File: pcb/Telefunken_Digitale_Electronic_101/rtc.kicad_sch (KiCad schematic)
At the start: 5 parts, among them U3 DS3231

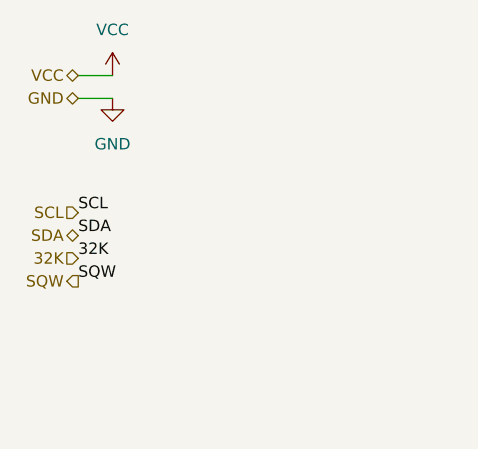
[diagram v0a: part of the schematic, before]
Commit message: SCH - rtc: adjusted footprints and direction of 32K label
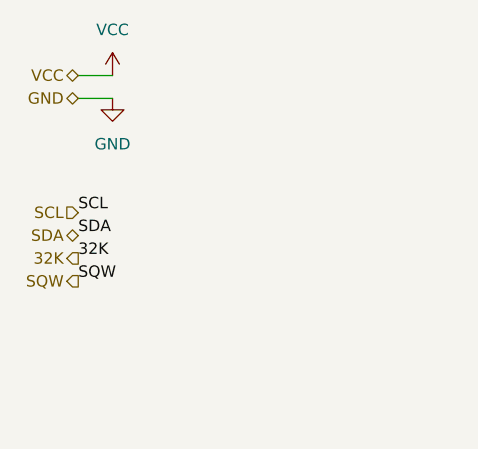
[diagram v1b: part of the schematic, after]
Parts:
- R10, R9: footprint Capacitor_SMD:C_0603_1608Metric_Pad1.08x0.95mm_HandSolder -> Resistor_SMD:R_0603_1608Metric_Pad0.98x0.95mm_HandSolder
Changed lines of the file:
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@@
 	)
 	(hierarchical_label "32K"
-		(shape input)
+		(shape output)
 		(at 38.1 77.47 180)
 		(effects
@@
 			)
 		)
-		(property "Footprint" "Capacitor_SMD:C_0603_1608Metric_Pad1.08x0.95mm_HandSolder"
+		(property "Footprint" "Resistor_SMD:R_0603_1608Metric_Pad0.98x0.95mm_HandSolder"
 			(at 136.652 78.74 90)
 			(hide yes)
@@
 			)
 		)
-		(property "Footprint" "Capacitor_SMD:C_0603_1608Metric_Pad1.08x0.95mm_HandSolder"
+		(property "Footprint" "Resistor_SMD:R_0603_1608Metric_Pad0.98x0.95mm_HandSolder"
 			(at 132.842 81.28 90)
 			(hide yes)

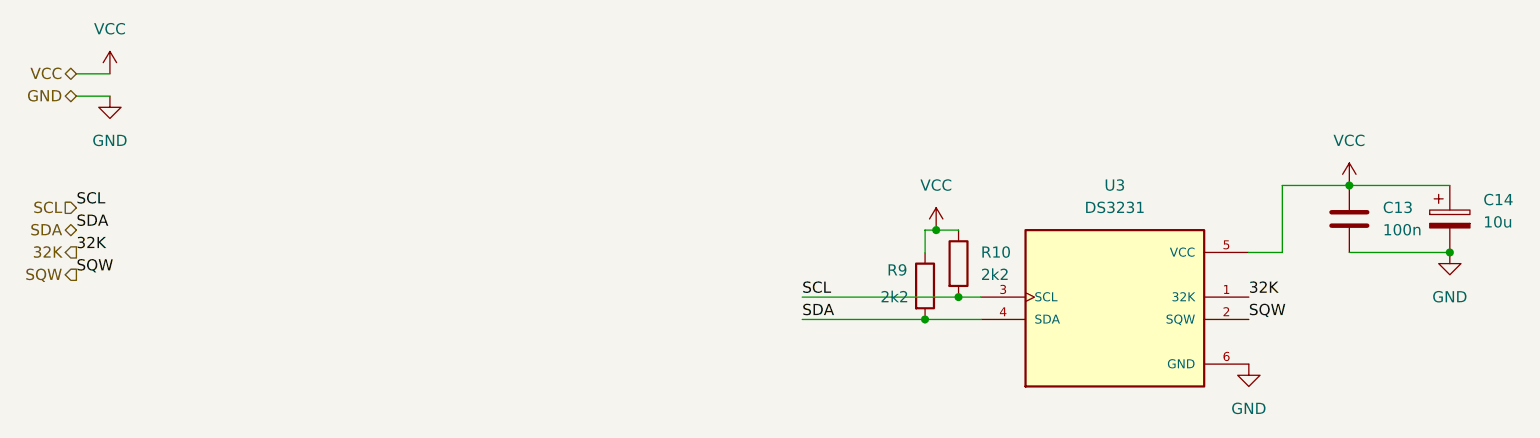
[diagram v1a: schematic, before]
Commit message: SCH and PCB: reannotated everything
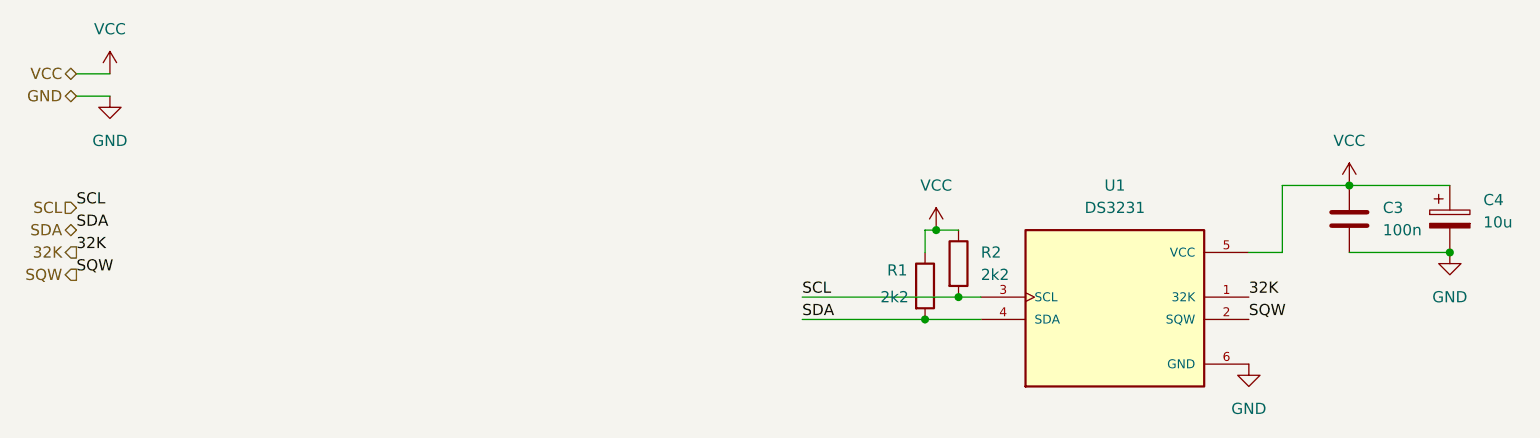
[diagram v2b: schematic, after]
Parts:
- renumbered C13 to C3, C14 to C4, R9 to R1, R10 to R2, U3 to U1
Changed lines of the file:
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@@
 		(dnp no)
 		(fields_autoplaced yes)
-		(property "Reference" "#PWR09"
+		(property "Reference" "#PWR013"
 			(at 194.31 83.82 0)
 			(hide yes)
@@
 			(project "Telefunken_Digitale_Electronic_101"
 				(path "/df1af5ff-c8b9-4769-9610-ead9e11e7e65/bbe7d115-46a0-489e-9136-389da3eb571d"
-					(reference "#PWR09")
+					(reference "#PWR013")
 					(unit 1)
 				)
@@
 		(dnp no)
 		(fields_autoplaced yes)
-		(property "Reference" "#PWR08"
+		(property "Reference" "#PWR012"
 			(at 182.88 73.66 0)
 			(hide yes)
@@
 			(project "Telefunken_Digitale_Electronic_101"
 				(path "/df1af5ff-c8b9-4769-9610-ead9e11e7e65/bbe7d115-46a0-489e-9136-389da3eb571d"
-					(reference "#PWR08")
+					(reference "#PWR012")
 					(unit 1)
 				)
@@
 		(dnp no)
 		(fields_autoplaced yes)
-		(property "Reference" "#PWR024"
+		(property "Reference" "#PWR09"
 			(at 41.91 66.04 0)
 			(hide yes)
@@
 			(project "Telefunken_Digitale_Electronic_101"
 				(path "/df1af5ff-c8b9-4769-9610-ead9e11e7e65/bbe7d115-46a0-489e-9136-389da3eb571d"
-					(reference "#PWR024")
+					(reference "#PWR09")
 					(unit 1)
 				)
@@
 		(dnp no)
 		(fields_autoplaced yes)
-		(property "Reference" "C13"
+		(property "Reference" "C3"
 			(at 186.69 72.3899 0)
 			(show_name no)
@@
 			(project "Telefunken_Digitale_Electronic_101"
 				(path "/df1af5ff-c8b9-4769-9610-ead9e11e7e65/bbe7d115-46a0-489e-9136-389da3eb571d"
-					(reference "C13")
+					(reference "C3")
 					(unit 1)
 				)
@@
 		(dnp no)
 		(fields_autoplaced yes)
-		(property "Reference" "#PWR019"
+		(property "Reference" "#PWR010"
 			(at 135.89 78.74 0)
 			(hide yes)
@@
 			(project "Telefunken_Digitale_Electronic_101"
 				(path "/df1af5ff-c8b9-4769-9610-ead9e11e7e65/bbe7d115-46a0-489e-9136-389da3eb571d"
-					(reference "#PWR019")
+					(reference "#PWR010")
 					(unit 1)
 				)
@@
 		(dnp no)
 		(fields_autoplaced yes)
-		(property "Reference" "R10"
+		(property "Reference" "R2"
 			(at 140.97 77.4699 0)
 			(show_name no)
@@
 			(project "Telefunken_Digitale_Electronic_101"
 				(path "/df1af5ff-c8b9-4769-9610-ead9e11e7e65/bbe7d115-46a0-489e-9136-389da3eb571d"
-					(reference "R10")
+					(reference "R2")
 					(unit 1)
 				)
@@
 		(dnp no)
 		(fields_autoplaced yes)
-		(property "Reference" "C14"
+		(property "Reference" "C4"
 			(at 198.12 71.5009 0)
 			(show_name no)
@@
 			(project "Telefunken_Digitale_Electronic_101"
 				(path "/df1af5ff-c8b9-4769-9610-ead9e11e7e65/bbe7d115-46a0-489e-9136-389da3eb571d"
-					(reference "C14")
+					(reference "C4")
 					(unit 1)
 				)
@@
 		(dnp no)
 		(fields_autoplaced yes)
-		(property "Reference" "U3"
+		(property "Reference" "U1"
 			(at 156.21 69.85 0)
 			(show_name no)
@@
 			(project "Telefunken_Digitale_Electronic_101"
 				(path "/df1af5ff-c8b9-4769-9610-ead9e11e7e65/bbe7d115-46a0-489e-9136-389da3eb571d"
-					(reference "U3")
+					(reference "U1")
 					(unit 1)
 				)
@@
 		(dnp no)
 		(fields_autoplaced yes)
-		(property "Reference" "#PWR010"
+		(property "Reference" "#PWR011"
 			(at 171.45 96.52 0)
 			(hide yes)
@@
 			(project "Telefunken_Digitale_Electronic_101"
 				(path "/df1af5ff-c8b9-4769-9610-ead9e11e7e65/bbe7d115-46a0-489e-9136-389da3eb571d"
-					(reference "#PWR010")
+					(reference "#PWR011")
 					(unit 1)
 				)
@@
 		(dnp no)
 		(fields_autoplaced yes)
-		(property "Reference" "#PWR023"
+		(property "Reference" "#PWR08"
 			(at 41.91 60.96 0)
 			(hide yes)
@@
 			(project "Telefunken_Digitale_Electronic_101"
 				(path "/df1af5ff-c8b9-4769-9610-ead9e11e7e65/bbe7d115-46a0-489e-9136-389da3eb571d"
-					(reference "#PWR023")
+					(reference "#PWR08")
 					(unit 1)
 				)
@@
 		(in_pos_files yes)
 		(dnp no)
-		(property "Reference" "R9"
+		(property "Reference" "R1"
 			(at 130.302 79.502 0)
 			(show_name no)
@@
 			(project "Telefunken_Digitale_Electronic_101"
 				(path "/df1af5ff-c8b9-4769-9610-ead9e11e7e65/bbe7d115-46a0-489e-9136-389da3eb571d"
-					(reference "R9")
-					(unit 1)
-				)
+					(reference "R1")
+					(unit 1)
+				)

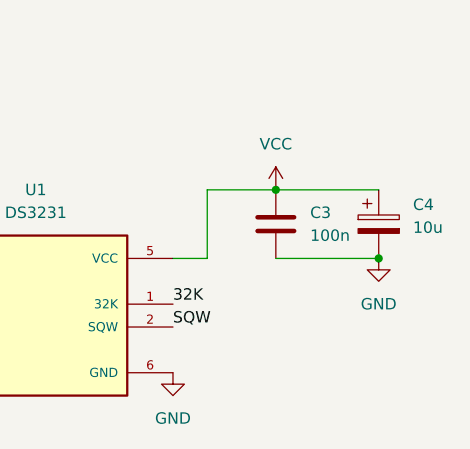
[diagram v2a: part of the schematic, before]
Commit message: adjusted connectors footprints, added footprint to input polarized capacitor, rtc and display polarized capacitors converted to non polarized
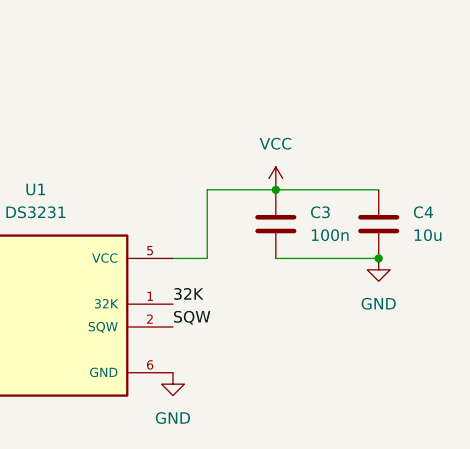
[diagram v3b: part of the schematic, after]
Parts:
- C4: symbol Device:C_Polarized -> Device:C
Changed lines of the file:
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@@
 	)
 	(symbol
-		(lib_id "Device:C_Polarized")
+		(lib_id "Device:C")
 		(at 194.31 73.66 0)
 		(unit 1)
@@
 		(fields_autoplaced yes)
 		(property "Reference" "C4"
-			(at 198.12 71.5009 0)
+			(at 198.12 72.3899 0)
 			(show_name no)
 			(do_not_autoplace no)
@@
 		)
 		(property "Value" "10u"
-			(at 198.12 74.0409 0)
+			(at 198.12 74.9299 0)
 			(show_name no)
 			(do_not_autoplace no)
@@
 			)
 		)
-		(property "Description" "Polarized capacitor"
+		(property "Description" "Unpolarized capacitor"
 			(at 194.31 73.66 0)
 			(hide yes)
